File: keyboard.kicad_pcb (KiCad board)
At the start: 2 copper layers, 233.1 x 83.1 mm, 92 parts, among them J1 Conn_01x04_Male, J4 Conn_01x11_Male, K0 KEYSW, K1 KEYSW, K10 KEYSW, K11 KEYSW, K12 KEYSW, K13 KEYSW, K14 KEYSW, K15 KEYSW, K16 KEYSW, K17 KEYSW, K18 KEYSW, K19 KEYSW, K2 KEYSW, K20 KEYSW, K21 KEYSW, K22 KEYSW, K23 KEYSW, K24 KEYSW, K25 KEYSW, K26 KEYSW, K27 KEYSW, K28 KEYSW, K29 KEYSW, K3 KEYSW, K30 KEYSW, K31 KEYSW, K32 KEYSW, K33 KEYSW, K34 KEYSW, K35 KEYSW, K36 KEYSW, K37 KEYSW, K38 KEYSW, K39 KEYSW, K4 KEYSW, K40 KEYSW, K41 KEYSW, K42 KEYSW, K43 KEYSW, K5 KEYSW, K6 KEYSW, K7 KEYSW, K8 KEYSW, K9 KEYSW

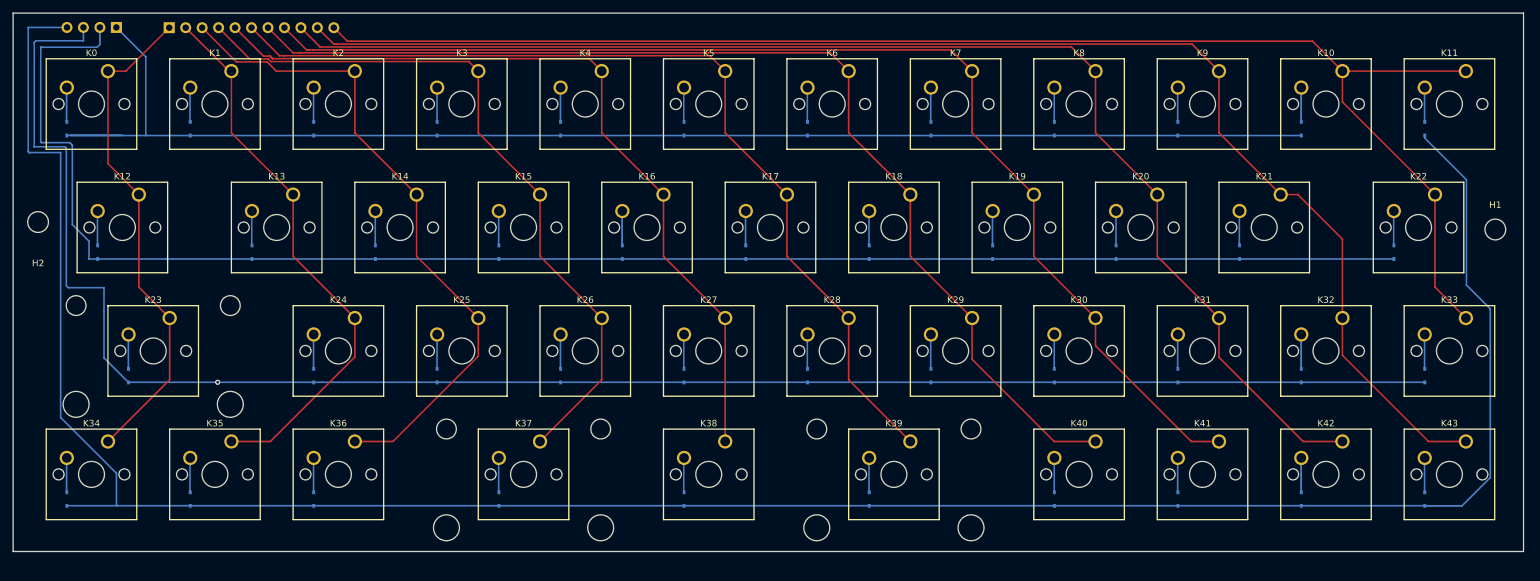
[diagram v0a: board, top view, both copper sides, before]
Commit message: Reroute board, better silkscreening and added images
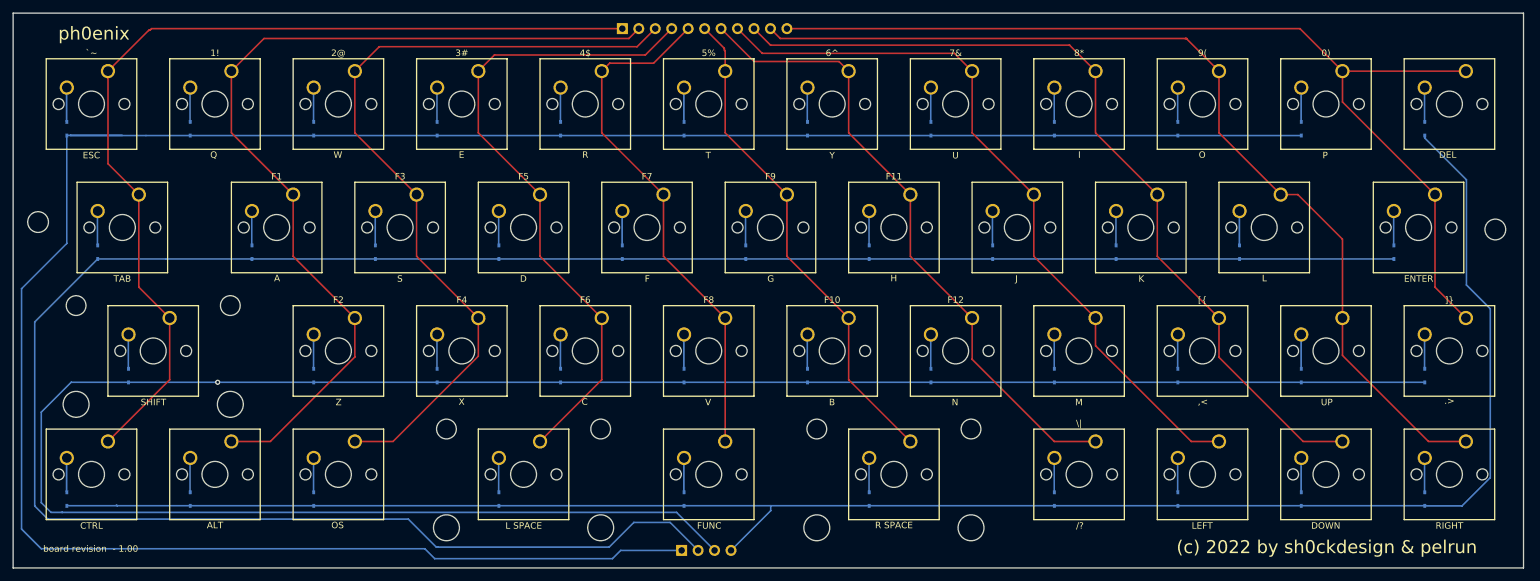
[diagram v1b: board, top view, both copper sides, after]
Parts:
- L SPACE: renamed from K37
- R SPACE: renamed from K39
- moved ROWS 118.8 mm to (198.4, 193.8), turned to -90 degrees
- moved COLUMNS 69.9 mm to (189.2, 113.3)
- renumbered K10 to 0), K1 to 1!, K2 to 2@, K3 to 3#, K4 to 4$, K5 to 5%, K6 to 6^, K7 to 7&, K8 to 8*, K9 to 9(, K35 to ALT, J4 to COLUMNS, K34 to CTRL, K11 to DEL, K42 to DOWN, K22 to ENTER, K13 to F1, K28 to F10, K18 to F11, K29 to F12, K24 to F2, K14 to F3, K25 to F4, K15 to F5, K26 to F6, K16 to F7, K27 to F8, K17 to F9, K38 to FUNC, K19 to J, K20 to K, K21 to L, K41 to LEFT, K30 to M, K36 to OS, K43 to RIGHT, J1 to ROWS, K23 to SHIFT, K12 to TAB, K32 to UP, K31 to [{, K40 to \|, K33 to ]}, K0 to `~
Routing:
- net /Row_0: track 217.0 -> 366.4 mm
- net /Row_1: track 251.6 -> 350.5 mm
- net /Row_3: track 366.8 -> 288.1 mm
- net /Col_7: track 184.6 -> 114.3 mm
- net /Col_8: track 201.9 -> 131.9 mm
- net /Col_6: track 169.0 -> 99.1 mm
- net /Col_10: track 223.5 -> 153.5 mm
- net /Col_0: track 77.3 -> 147.1 mm
- net /Col_9: track 219.8 -> 150.1 mm
- net /Col_5: track 144.9 -> 76.9 mm
- net /Row_2: track 274.3 -> 336.5 mm
- net /Col_1: track 86.3 -> 142.4 mm
- net /Col_4: track 125.1 -> 81.1 mm
- net /Col_2: track 102.7 -> 125.5 mm
- net /Col_3: track 111.8 -> 101.5 mm
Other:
- board size 233.1 x 83.1 mm -> 233.1 x 85.6 mm
- board text added: "(c) 2022 by sh0ckdesign & pelrun"
- board text added: ",<"
- board text added: ".>"
- board text added: "/?"
- board text added: "A"
- board text added: "B"
- board text added: "C"
- board text added: "D"
- board text added: "E"
- board text added: "ESC"
- board text added: "F"
- board text added: "G"
- board text added: "H"
- board text added: "I"
- board text added: "N"
- board text added: "O"
- board text added: "P"
- board text added: "Q"
- board text added: "R"
- board text added: "S"
- board text added: "T"
- board text added: "U"
- board text added: "V"
- board text added: "W"
- board text added: "X"
- board text added: "Y"
- board text added: "Z"
- board text added: "board revision - 1.00"
- board text added: "ph0enix"
- board text removed: "ph0en1x by sh0ckdesign & pelrun - revision 1.0"
